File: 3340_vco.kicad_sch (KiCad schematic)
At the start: 68 parts, among them J1 1V/OCT IN, J1 CV2 IN, J1 EXT PWM CONTROL IN, J1 FM IN, J1 SAW OUT, J1 SQ OUT, J1 SYNC IN, J1 TRI OUT, J4 Conn_01x10, SW1 OCTAVES, SW2 SYNC_TYPE, U1 AS3340, U2 TL074

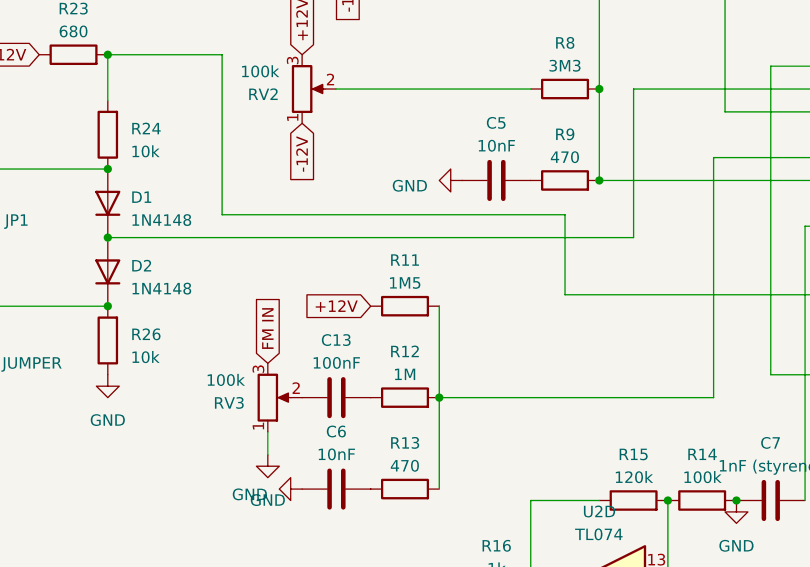
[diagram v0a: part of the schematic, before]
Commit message: BOM updated with correct resistor values
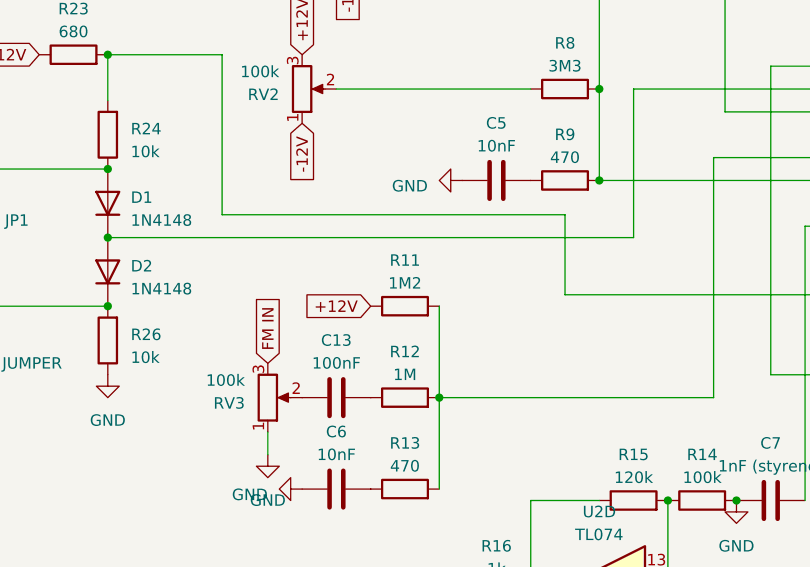
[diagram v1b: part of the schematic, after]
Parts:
- R11: value 1M5 -> 1M2
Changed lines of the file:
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@@
       (effects (font (size 1.27 1.27)))
     )
-    (property "Value" "1M5" (at 134.62 102.87 90)
+    (property "Value" "1M2" (at 134.62 102.87 90)
       (effects (font (size 1.27 1.27)))
     )
